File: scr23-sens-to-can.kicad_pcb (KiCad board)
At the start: 2 copper layers, 61 parts, among them J1 ATM13-12PA-BM01, SW1 SW_SPDT, U1 SRV05-4, U10 AP63205WU, U2 MCP6004, U3 MCP6004, U4 TJA1042T-3, U5 AP7370-33Y-13, U8 STM32G431CBT6, U9 SRV05-4

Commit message: layout & traces in progress
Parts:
- moved H3 83.6 mm to (164.1, 107.2)
- moved D1 75.1 mm to (165.6, 75.5), turned to 90 degrees
- moved C19 65.9 mm to (135.7, 80.5)
- moved C9 59.4 mm to (132.4, 83.1), turned to -90 degrees
- moved C8 57.0 mm to (124.8, 93.7), turned to -90 degrees
- moved H2 56.9 mm to (124.2, 107.2)
- moved C21 56.5 mm to (175.3, 123.4)
- moved U5 54.5 mm to (162.3, 95.8), turned to -90 degrees
- moved D11 54.3 mm to (155.5, 92.4), turned to 90 degrees
- moved C28 50.7 mm to (147.5, 80.5)
- moved H4 46.9 mm to (124.2, 77.5)
- moved C20 45.6 mm to (154.4, 75.8), turned to 90 degrees
- moved C25 43.8 mm to (154.3, 81.5), turned to -90 degrees
- moved C7 42.5 mm to (140.1, 105.2), turned to 90 degrees
- moved C6 42.5 mm to (127.0, 93.7), turned to -90 degrees
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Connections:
- U1 pad 1: A0 -> A5
- U1 pad 3: A1 -> A4
- U1 pad 4: A2 -> A1
- U1 pad 6: A3 -> A0
- U9 pad 1: A4 -> A3
- U9 pad 3: A5 -> A2
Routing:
- net GND: track 0.00 -> 99.6 mm, vias 0 -> 23
- net ADC2_IN4: track 0.00 -> 24.0 mm, vias 0 -> 2
- net ADC2_IN3: track 0.00 -> 22.3 mm, vias 0 -> 2
- net +3.3V: track 0.00 -> 20.5 mm, vias 0 -> 2
- net ADC2_IN13: track 0.00 -> 16.2 mm, vias 0 -> 2
- net A3: track 0.00 -> 15.1 mm
- net +3.3VA: track 0.00 -> 14.1 mm
- net A0: track 0.00 -> 10.6 mm, vias 0 -> 2
- net A2: track 0.00 -> 9.96 mm
- net Net-(C25-Pad1): track 0.00 -> 9.34 mm
- net ADC1_IN2: track 0.00 -> 9.11 mm
- net A5: track 0.00 -> 9.01 mm
- net ADC1_IN3: track 0.00 -> 8.55 mm
- net FDCAN1_TX: track 0.00 -> 8.31 mm
- net Net-(R13-Pad2): track 0.00 -> 8.07 mm
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- added copper zone on F.Cu, net +3.3V
- added copper zone on F.Cu, net +5V
- added copper zone on B.Cu, net GND

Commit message: layout progress
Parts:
- moved H1 79.2 mm to (170.7, 108.7)
- moved C22 52.2 mm to (138.2, 75.7), turned to 90 degrees
- moved H3 51.7 mm to (121.9, 77.2)
- moved H4 46.5 mm to (170.7, 77.2)
- moved D2 39.9 mm to (123.4, 88.4), turned to -90 degrees
- moved C4 39.5 mm to (136.1, 117.3)
- moved C17 36.5 mm to (137.4, 121.4)
- moved C21 36.5 mm to (138.9, 126.6)
- moved C23 36.5 mm to (143.0, 120.9)
- moved C16 27.3 mm to (154.9, 108.2)
- moved J1 4.17 mm to (115.3, 84.1)
- moved H2 2.75 mm to (121.9, 108.7)
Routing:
- net +5V: track 5.18 -> 87.5 mm, vias 0 -> 2
- net +12V: track 3.65 -> 65.3 mm, vias 0 -> 2
- net A3: track 15.1 -> 68.2 mm, vias 0 -> 1
- net A6: track 7.64 -> 60.8 mm, vias 0 -> 1
- net CANH: track 0.00 -> 41.0 mm, vias 0 -> 2
- net A2: track 9.96 -> 48.7 mm, vias 0 -> 1
- net CANL: track 0.00 -> 38.3 mm, vias 0 -> 2
- net A4: track 4.52 -> 26.0 mm, vias 0 -> 1
- net A5: track 9.01 -> 26.0 mm
- net A1: track 5.55 -> 21.1 mm, vias 0 -> 1
- net A0: track 10.6 -> 18.9 mm
- net GND: track 99.6 -> 104.8 mm, vias 23 -> 24
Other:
- board outline added: 78.7 x 42.9 mm
- board text added: "SC Racing CAN Module"

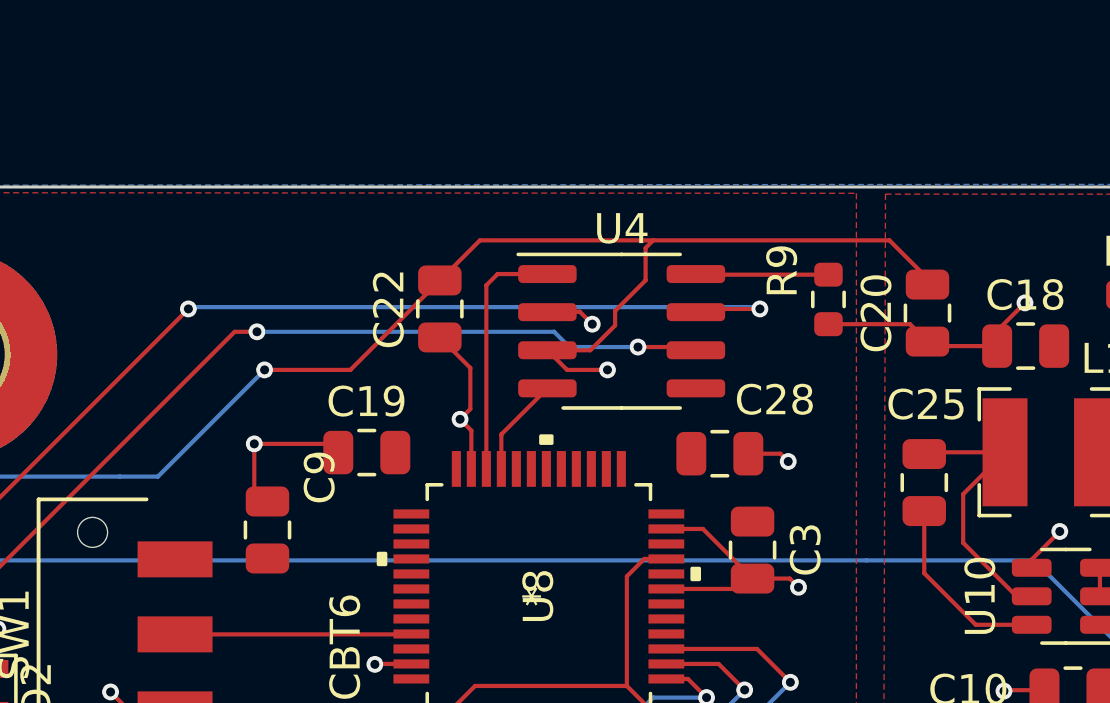
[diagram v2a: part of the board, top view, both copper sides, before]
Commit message: rotate tranceiver
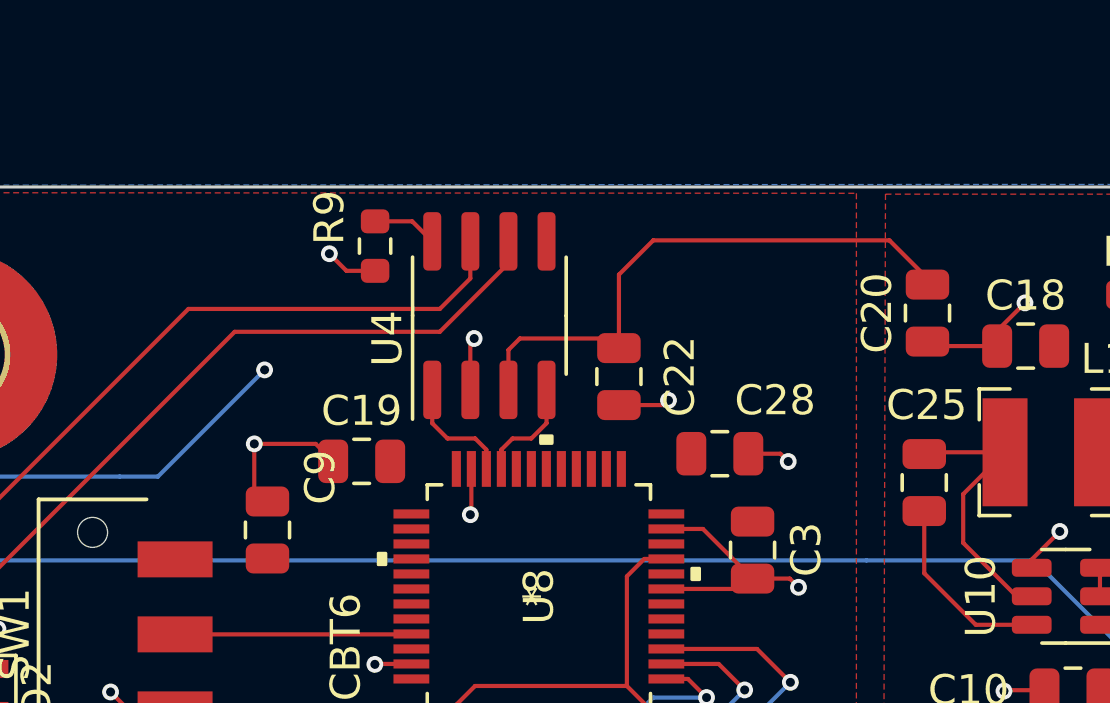
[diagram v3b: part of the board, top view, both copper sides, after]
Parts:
- moved R9 15.2 mm to (136.0, 73.6)
- moved C22 6.38 mm to (144.1, 77.9)
- moved U4 4.44 mm to (139.8, 75.9), turned to 90 degrees
- moved C19 0.34 mm to (135.6, 80.8)
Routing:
- net +5V: track 87.5 -> 73.9 mm, vias 2 -> 1
- net CANH: track 41.0 -> 30.7 mm, vias 2 -> 0
- net CANL: track 38.3 -> 33.5 mm, vias 2 -> 0
- net FDCAN1_TX: track 8.31 -> 3.92 mm
- net GND: track 104.8 -> 101.2 mm, vias 24 -> 26
- net CAN_STB: track 4.43 -> 2.18 mm

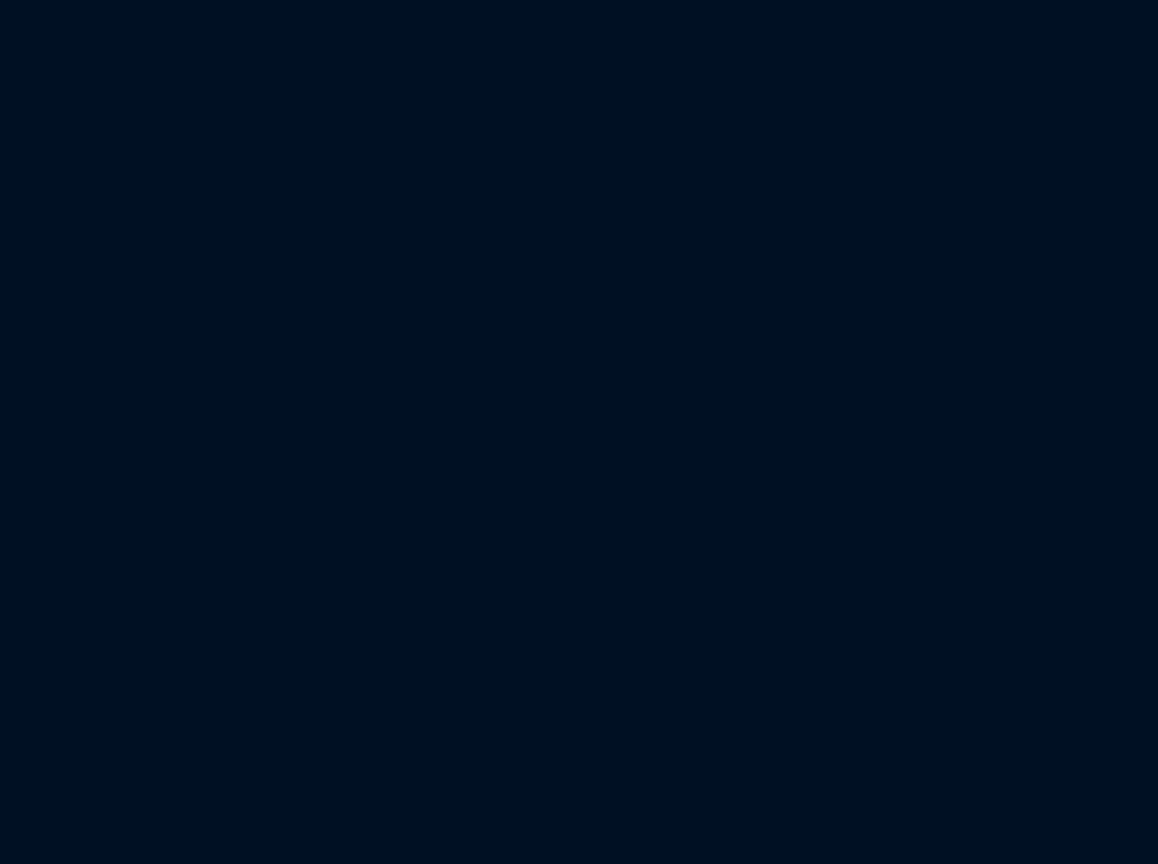
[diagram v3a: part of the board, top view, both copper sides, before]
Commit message: switch to external ADC, switch to amp superseal 1.0 for connector, need to check CANFD pins disagreement with datasheet
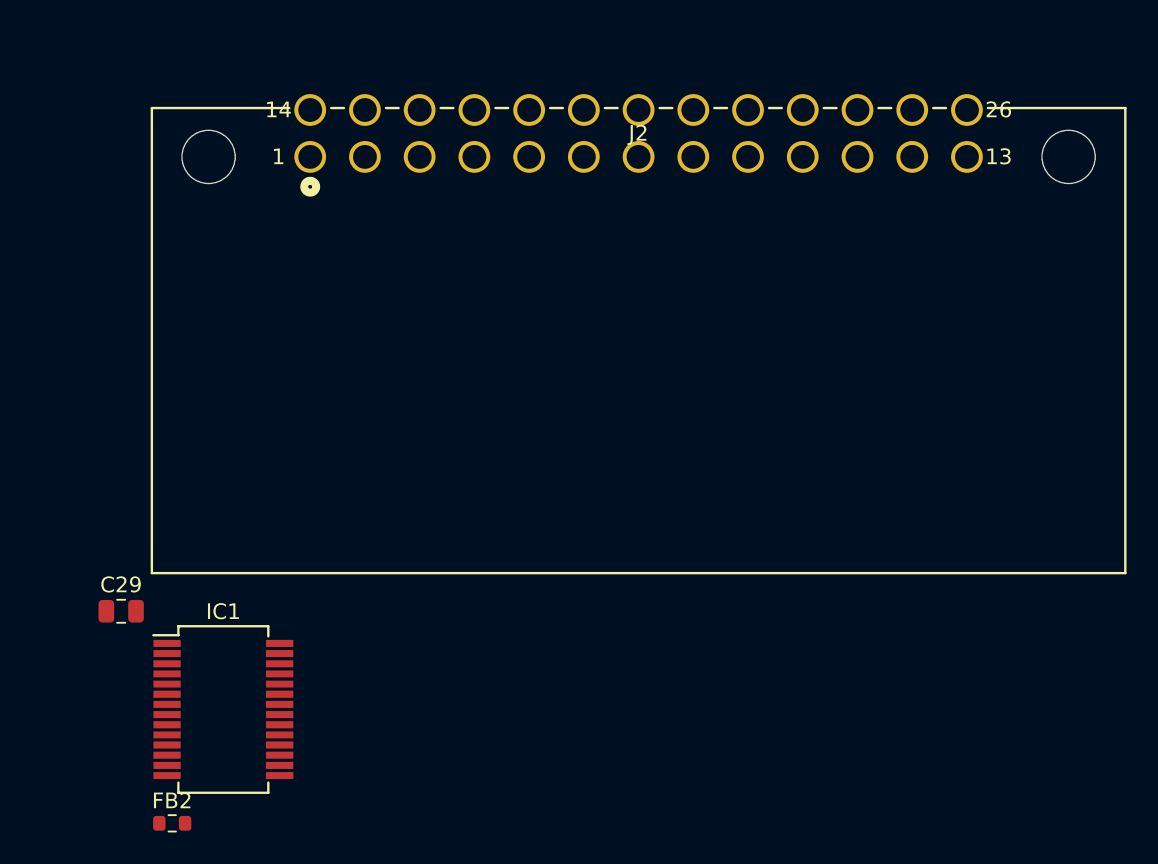
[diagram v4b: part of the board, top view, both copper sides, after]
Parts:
- added C29: 100uF, Capacitor_SMD:C_0805_2012Metric, F.Cu at (206.9, 145.3)
- added FB2: 400, Resistor_SMD:R_0603_1608Metric, F.Cu at (210.1, 158.9)
- added IC1: ADS1256IDBRG4, Package_SO:SSOP-28_5.3x10.2mm_P0.65mm, F.Cu at (213.4, 151.6)
- added J2: 6473711-1, CON26_2X13_SUPERSEAL_TYC:CON26_2X13_SUPERSEAL_TYC, F.Cu at (219.0, 116.3)
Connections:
- U8 pad 10: ADC1_IN3 -> D1
- U8 pad 11: ADC1_IN4 -> unconnected-(U8A-PA3-Pad11)
- U8 pad 13: ADC2_IN13 -> SPI1_SCK
- U8 pad 14: ADC2_IN3 -> SPI1_MISO
- U8 pad 15: ADC2_IN4 -> SPI1_MOSI
- U8 pad 25: unconnected-(U8-Pad25) -> USB_DM
- U8 pad 26: unconnected-(U8-Pad26) -> USB_DP
- U8 pad 41: unconnected-(U8-Pad41) -> UCPD1_CC2
- U8 pad 43: unconnected-(U8-Pad43) -> UCPD1_CC1
- U8 pad 8: ADC1_IN1 -> unconnected-(U8A-PA0-Pad8)
- U8 pad 9: ADC1_IN2 -> D0
